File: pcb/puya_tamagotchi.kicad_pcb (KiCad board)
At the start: 2 copper layers, 40 x 59.5 mm, 49 parts, among them J1 SWD pins, J2 ADDITIONAL, J3 BATTERY, J4 USB_C_Receptacle_PowerOnly_6P, Q1 AO3400A, Q2 AO3400A, Q3 AO3400A, Q4 AO3401A, SW1 TS-1187A-B-A-B, SW2 TS-1187A-B-A-B, SW3 TS-1187A-B-A-B, SW4 TS-1187A-B-A-B, U1 PY32F002BF15U6TR, U2 OLED_128x64_SSD1306, U3 TP4056, U4 DW01A

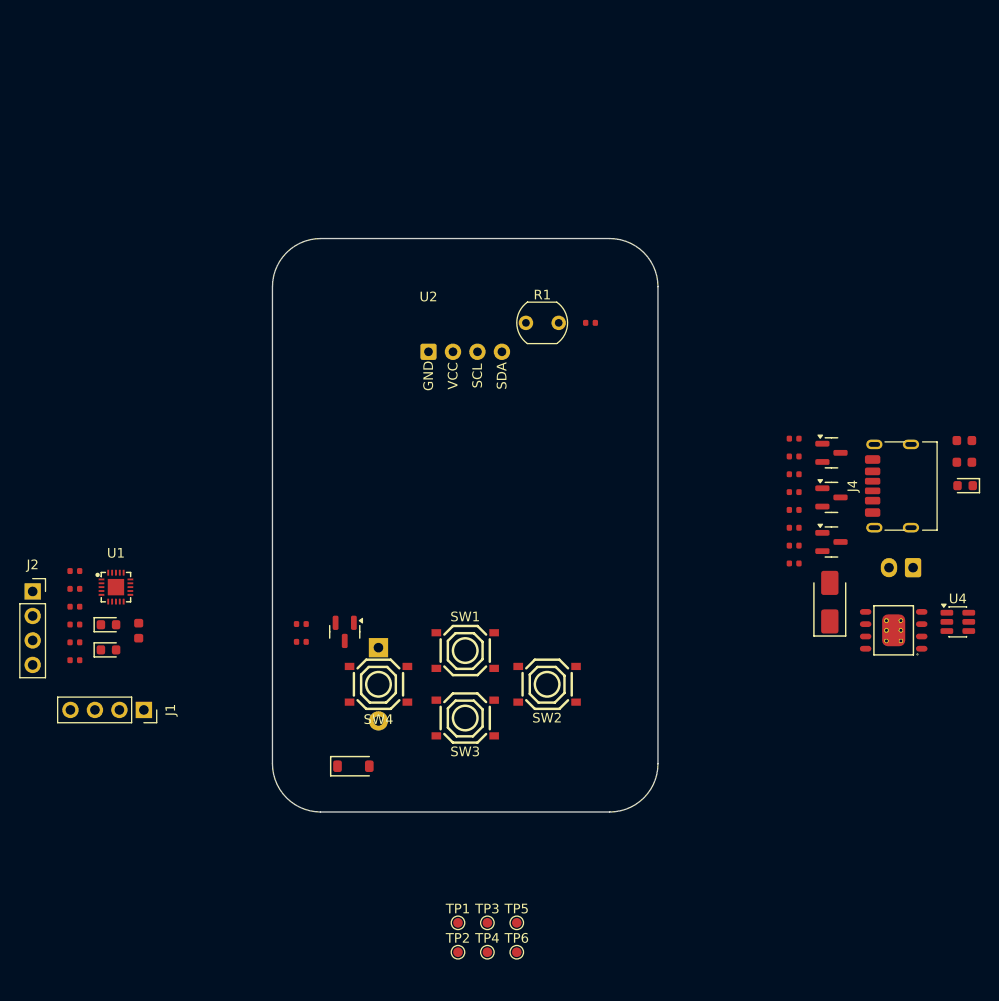
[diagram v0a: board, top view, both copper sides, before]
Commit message: Outline component placement
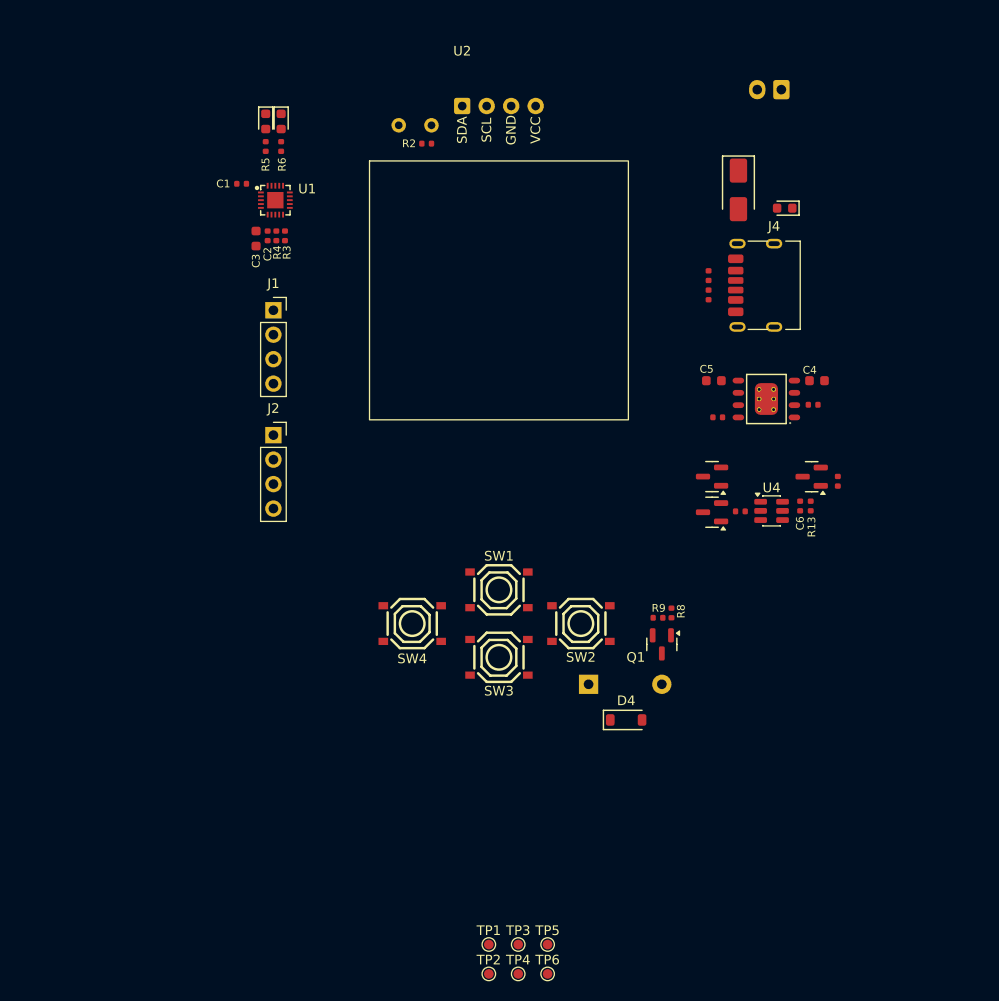
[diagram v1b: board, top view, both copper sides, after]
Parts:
- R1: moved to B.Cu
- U2: value OLED_128x64_SSD1306 -> OLED_SH1107_128X128; footprint Tamagotchi_footprints:SSD1306_OLED -> Tamagotchi_footprints:SH1107_128x128_OLED
- moved D3 57.7 mm to (67.4, 35.6), turned to -90 degrees
- moved R6 57.4 mm to (67.4, 38.2), turned to 90 degrees
- moved R5 55.1 mm to (65.8, 38.2), turned to 90 degrees
- moved D2 54.7 mm to (65.8, 35.6), turned to -90 degrees
- moved J3 51.4 mm to (119.3, 32.3)
- moved R4 45.4 mm to (66.9, 47.5), turned to -90 degrees
- moved R3 44.2 mm to (67.8, 47.5), turned to -90 degrees
- moved D5 43.8 mm to (114.8, 42.7), turned to -90 degrees
- moved C1 43.7 mm to (63.3, 42.1)
- moved J1 43.6 mm to (66.6, 55.2), turned to 0 degrees
- moved U1 43.4 mm to (66.8, 43.8)
- moved C3 42.5 mm to (64.8, 47.7)
- moved C2 41.7 mm to (66.0, 47.5), turned to 90 degrees
- moved R8 38.4 mm to (107.9, 86.6), turned to -90 degrees
- moved R9 37.1 mm to (106.5, 87.1), turned to 180 degrees
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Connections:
- U2 pad 1: GND -> /I2C.SDA
- U2 pad 2: VCC -> /I2C.SCL
- U2 pad 3: /I2C.SCL -> GND
- U2 pad 4: /I2C.SDA -> VCC
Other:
- board outline removed

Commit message: Align components, add edgecuts
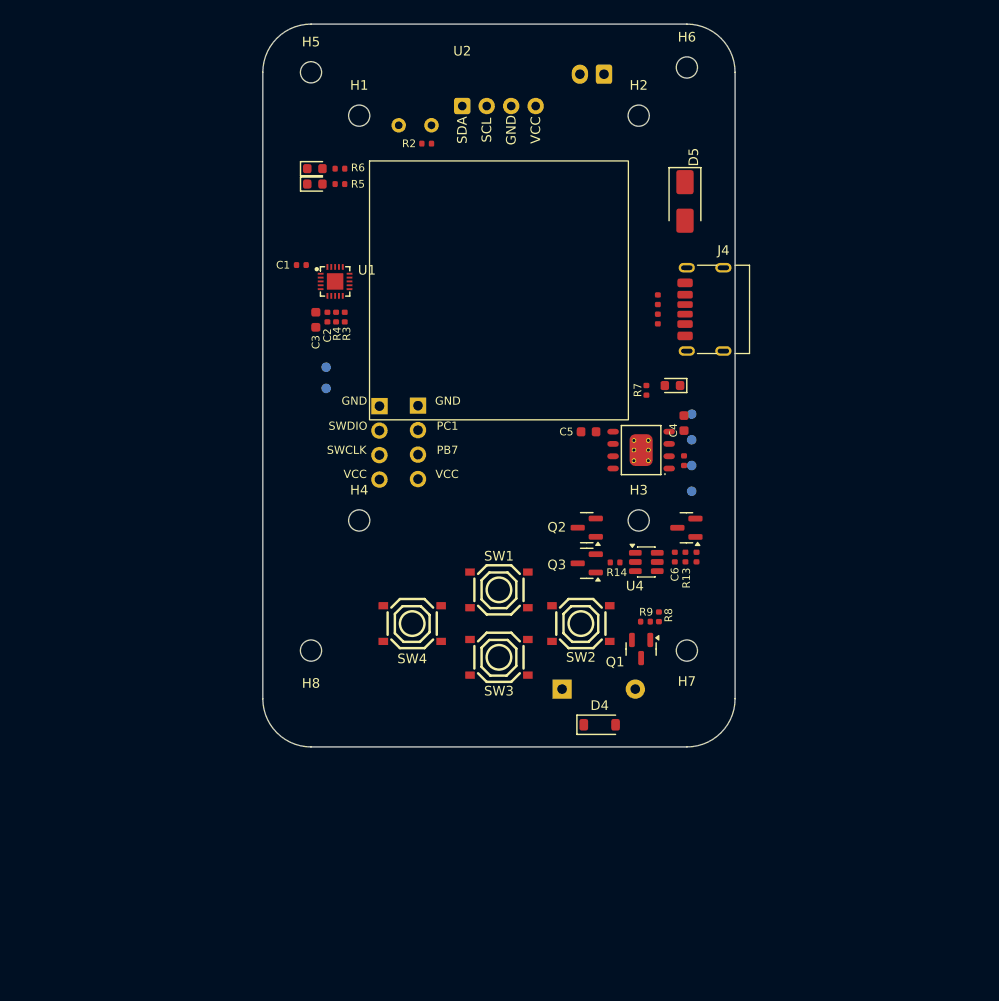
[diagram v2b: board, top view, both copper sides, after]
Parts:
- added H1: MountingHole, MountingHole:MountingHole_2.2mm_M2, F.Cu at (75.5, 35.0)
- added H2: MountingHole, MountingHole:MountingHole_2.2mm_M2, F.Cu at (104.5, 35.0)
- added H3: MountingHole, MountingHole:MountingHole_2.2mm_M2, F.Cu at (104.5, 77.0)
- added H4: MountingHole, MountingHole:MountingHole_2.2mm_M2, F.Cu at (75.5, 77.0)
- added H5: MountingHole, MountingHole:MountingHole_2.2mm_M2, F.Cu at (70.5, 30.5)
- added H6: MountingHole, MountingHole:MountingHole_2.2mm_M2, F.Cu at (109.5, 30.0)
- added H7: MountingHole, MountingHole:MountingHole_2.2mm_M2, F.Cu at (109.5, 90.5)
- added H8: MountingHole, MountingHole:MountingHole_2.2mm_M2, F.Cu at (70.5, 90.5)
- J1, J2, TP1, TP2, TP3, TP4, TP5, TP6: moved to B.Cu
- moved TP6 67.0 mm to (72.1, 61.1), turned to 180 degrees
- moved TP5 62.1 mm to (72.1, 63.3), turned to 180 degrees
- moved TP4 60.8 mm to (110.0, 66.0)
- moved TP2 56.8 mm to (110.0, 71.3)
- moved TP3 55.4 mm to (110.0, 68.6)
- moved TP1 51.5 mm to (110.0, 74.0)
- moved D1 21.8 mm to (108.0, 63.0)
- moved J3 18.5 mm to (100.9, 30.7)
- moved R15 16.6 mm to (110.5, 80.8), turned to 90 degrees
- moved J2 15.3 mm to (81.6, 65.1), turned to 180 degrees
- moved J1 14.8 mm to (77.6, 65.1), turned to 180 degrees
- moved R12 14.6 mm to (109.2, 70.8), turned to -90 degrees
- moved C4 14.5 mm to (109.2, 66.9), turned to -90 degrees
- moved C5 14.0 mm to (99.3, 67.8)
- moved C6 14.0 mm to (108.2, 80.8)
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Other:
- board outline added: 49 x 75 mm
- board text added: "+BATT"
- board text added: "GND"
- board text added: "PB7"
- board text added: "PC1"
- board text added: "SCL"
- board text added: "SDA"
- board text added: "SWCLK"
- board text added: "SWDIO"
- board text added: "VBUS"
- board text added: "VCC"

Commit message: Wire signals
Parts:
- moved R6 20.8 mm to (69.8, 61.0)
- moved D3 20.8 mm to (67.3, 61.0)
- moved TP5 19.6 mm to (67.1, 44.3)
- moved R5 17.6 mm to (69.8, 59.3)
- moved D2 17.6 mm to (67.3, 59.3)
- moved TP6 15.3 mm to (67.1, 46.6)
- moved R3 10.5 mm to (71.8, 45.6), turned to 180 degrees
- moved R4 10.3 mm to (73.8, 45.6), turned to 0 degrees
- moved C3 9.11 mm to (75.6, 48.3), turned to -90 degrees
- moved C2 7.62 mm to (74.4, 48.6), turned to -90 degrees
- moved R1 7.32 mm to (79.1, 28.7)
- moved R2 7.32 mm to (82.0, 30.6)
- moved C1 7.16 mm to (76.0, 53.5), turned to 90 degrees
- turned U1 to 180 degrees
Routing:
- net /BUZZER: track 0.00 -> 75.7 mm, vias 0 -> 2
- net /BUTTON_2: track 0.00 -> 56.1 mm, vias 0 -> 2
- net /BUTTON_3: track 0.00 -> 50.1 mm, vias 0 -> 2
- net /BUTTON_1: track 0.00 -> 43.8 mm, vias 0 -> 2
- net /LDR_OUT: track 0.00 -> 38.3 mm, vias 0 -> 1
- net /LDR_DRIVE: track 0.00 -> 36.7 mm, vias 0 -> 1
- net /BUTTON_4: track 0.00 -> 33.9 mm, vias 0 -> 2
- net /I2C.SCL: track 0.00 -> 33.9 mm, vias 0 -> 1
- net /I2C.SDA: track 0.00 -> 31.7 mm, vias 0 -> 1
- net /PB7: track 0.00 -> 22.9 mm, vias 0 -> 1
- net /SWCLK: track 0.00 -> 22.6 mm
- net /SWDIO: track 0.00 -> 21.6 mm
- net /PC1: track 0.00 -> 19.6 mm, vias 0 -> 1
- net Net-(U1-PA1): track 0.00 -> 10.8 mm
- net Net-(U1-PA0): track 0.00 -> 9.81 mm
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
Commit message: Wire whole board
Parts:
- moved D1 4.28 mm to (112.2, 63.8)
- moved R7 3.81 mm to (109.1, 63.8), turned to 0 degrees
- moved C4 2.71 mm to (106.9, 65.5), turned to 0 degrees
- moved BZ1 1.40 mm to (96.5, 93.1)
- moved R11 0.71 mm to (106.0, 55.6), turned to 180 degrees
- moved R10 0.71 mm to (106.0, 54.6), turned to 180 degrees
- moved C1 0.40 mm to (76.0, 53.9)
- moved Q4 0.30 mm to (109.5, 77.5), turned to -90 degrees
- moved J4 0.14 mm to (112.3, 55.1)
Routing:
- net VCC: track 1.00 -> 36.5 mm, vias 1 -> 4
- net Net-(U3-CHRG#): track 0.00 -> 16.5 mm, vias 0 -> 2
- net +BATT: track 0.00 -> 15.9 mm, vias 0 -> 3
- net GND: track 2.84 -> 18.2 mm, vias 4 -> 11
- net /VBUS: track 0.00 -> 14.5 mm, vias 0 -> 1
- net -BATT: track 0.00 -> 12.7 mm, vias 0 -> 2
- net Net-(Q2-G): track 0.00 -> 4.79 mm
- net Net-(Q3-G): track 0.00 -> 4.16 mm
- net Net-(Q2-D): track 0.00 -> 3.70 mm
- net Net-(U4-VCC): track 0.00 -> 2.93 mm
- net Net-(J4-CC2): track 0.00 -> 2.68 mm
- net Net-(J4-CC1): track 0.00 -> 2.68 mm
- net Net-(D1-Pad2): track 0.00 -> 1.81 mm
- net Net-(U4-CS): track 0.00 -> 1.62 mm
- net Net-(U3-PROG): track 0.00 -> 1.56 mm
- added copper zone on B.Cu, net +BATT
- added copper zone on B.Cu, net -BATT
- added copper zone on F.Cu, net /VBUS
- added copper zone on B.Cu, net GND
- added copper zone on F.Cu, net GND
- added copper zone on F.Cu, net VCC

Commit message: Update routing
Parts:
- added C7: 100nF, PCM_JLCPCB:C_0402, F.Cu at (92.6, 31.6)
- added R16: 10kΩ, PCM_JLCPCB:R_0402, F.Cu at (80.1, 60.8)
- added R17: 10kΩ, PCM_JLCPCB:R_0402, F.Cu at (76.6, 60.8)
- added TP7: TestPoint, TestPoint:TestPoint_Pad_D1.0mm, B.Cu at (85.2, 30.6)
- moved D4 2.60 mm to (100.5, 95.6)
- moved SW3 2.00 mm to (90.0, 93.2)
- moved TP5 1.14 mm to (68.2, 44.0)
- moved SW2 1.00 mm to (98.5, 88.7)
- moved SW4 1.00 mm to (81.0, 88.7)
- moved TP6 1.00 mm to (68.1, 46.6)
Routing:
- net /BUTTON_1: track 43.8 -> 79.2 mm, vias 2 -> 0
- net /BUZZER: track 75.7 -> 93.2 mm, vias 2 -> 0
- net VCC: track 36.5 -> 48.2 mm, vias 4 -> 3
- net /BUTTON_2: track 56.1 -> 62.3 mm, vias 2 -> 0
- net /BUTTON_4: track 33.9 -> 37.7 mm, vias 2 -> 0
- net /SWCLK: track 22.6 -> 25.6 mm, vias 0 -> 2
- net Net-(BZ1--): track 8.02 -> 5.42 mm
- net /I2C.SDA: track 31.7 -> 30.7 mm
- net /LDR_OUT: track 38.3 -> 39.3 mm, vias 1 -> 2
- net /I2C.SCL: track 33.9 -> 32.9 mm
- net /LDR_DRIVE: track 36.7 -> 37.3 mm, vias 1 -> 2
- net GND: track 18.2 -> 18.7 mm, vias 11 -> 28
- net /BUTTON_3: track 50.1 -> 49.7 mm, vias 2 -> 0
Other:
- board text added: "LDR_OUT"

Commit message: Add battery and usb silkscreen
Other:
- board text added: "+"
- board text added: "-"
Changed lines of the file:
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@@
 		(tags "resistor")
 		(property "Reference" "R10"
-			(at -1.05 -0.85 0)
+			(at -1.209999 0.999999 0)
 			(layer "F.SilkS")
-			(hide yes)
 			(effects
 				(font
@@
 		)
 		(property "Value" "5.1kΩ"
-			(at 0 0.199999 0)
+			(at 0 1.799999 0)
 			(layer "F.Fab")
-			(hide yes)
 			(effects
 				(font
@@
 		(tags "resistor")
 		(property "Reference" "R11"
-			(at -1.05 -0.85 0)
+			(at -1.209999 -1.199999 0)
 			(layer "F.SilkS")
-			(hide yes)
 			(effects
 				(font
@@
 		)
 		(property "Value" "5.1kΩ"
-			(at 0 0.199999 0)
+			(at -0.009999 -1.999999 0)
 			(layer "F.Fab")
-			(hide yes)
 			(effects
 				(font
@@
 		(layer "Edge.Cuts")
 	)
+	(gr_text "-"
+		(at 97.8 28.6 0)
+		(layer "F.SilkS")
+		(effects
+			(font
+				(size 0.85 0.85)
+				(thickness 0.15)
+				(bold yes)
+			)
+			(justify left bottom)
+		)
+	)
+	(gr_text "+"
+		(at 100.2 28.6 0)
+		(layer "F.SilkS")
+		(effects
+			(font
+				(size 0.85 0.85)
+				(thickness 0.15)
+				(bold yes)
+			)
+			(justify left bottom)
+		)
+	)
 	(gr_text "SWCLK\n"
 		(at 73.725 69.7 0)
@@
 		(layer "B.SilkS")
 		(effects
+			(font
+				(size 0.85 0.85)
+				(thickness 0.15)
+				(bold yes)
+			)
+			(justify left bottom mirror)
+		)
+	)
+	(gr_text "-"
+		(at 99 28.6 0)
+		(layer "B.SilkS")
+		(effects
+			(font
+				(size 0.85 0.85)
+				(thickness 0.15)
+				(bold yes)
+			)
+			(justify left bottom mirror)
+		)
+	)
+	(gr_text "+"
+		(at 101.4 28.6 0)
+		(layer "B.SilkS")
+		(effects
